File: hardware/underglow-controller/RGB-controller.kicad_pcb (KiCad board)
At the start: 4 copper layers, 86 x 97.7 mm, 142 parts, among them J2 U.FL-R-SMT-1(10), J3 DM3AT-SF-PEJM5, J4 DTM1312PA12PBR008, J5 Conn_01x10, J6 CONSOLE, J7 U.FL-R-SMT-1(10), J8 JTAG, Q2 Q_Dual_NMOS_S1G1S2G2D2D2D1D1, Q3 Q_Dual_NMOS_S1G1S2G2D2D2D1D1, Q4 Q_Dual_NMOS_S1G1S2G2D2D2D1D1, SW2 SW_Push, SW3 SW_Push, SW4 SW_Push, U10 DRV8844PWP, U11 RP2040, U2 ESP-PSRAM32, U3 SN65HVD230, U4 ESP32-S3R2, U5 W25Q128JVS, U6 WS2815B, U7 W25Q128JVS, U8 ADP2303ARDZ-3.3, U9 COM-13909, Y2 40MHZ, Y3 32.7k, Y4 40MHZ

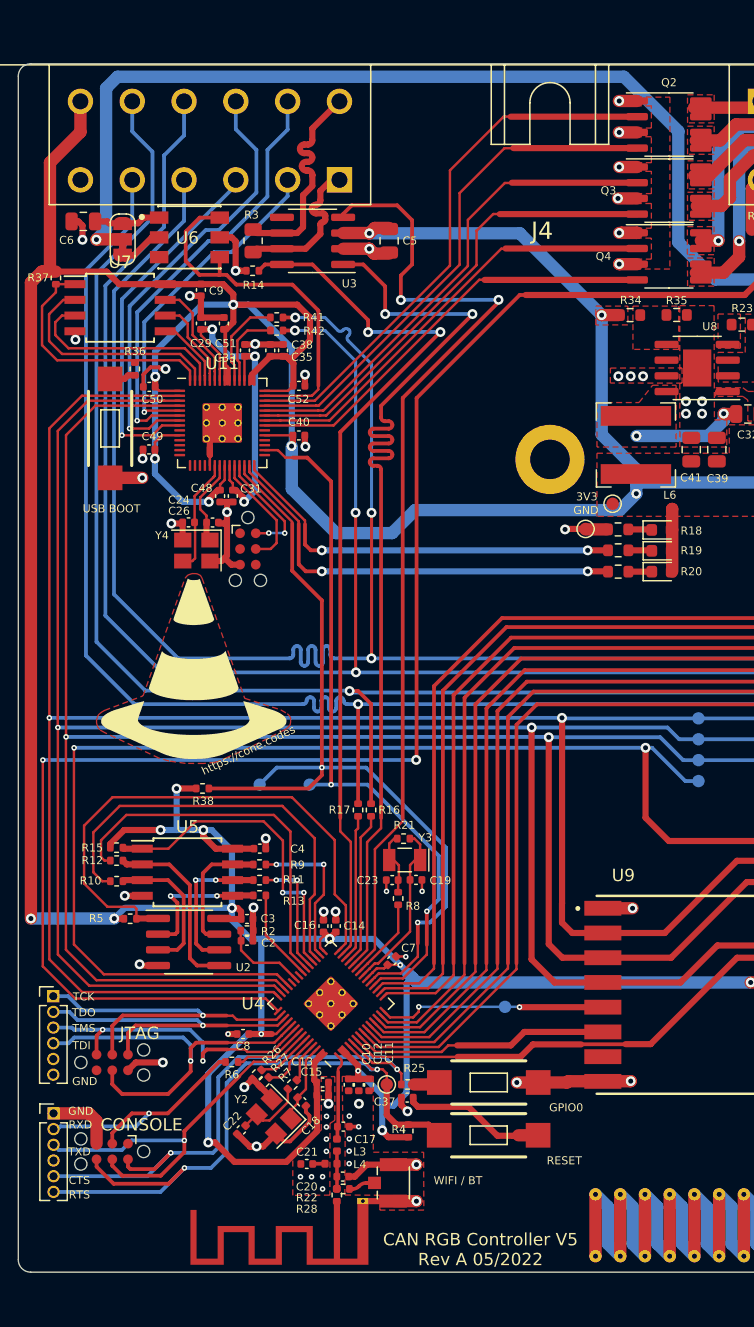
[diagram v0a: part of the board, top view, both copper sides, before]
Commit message: Update images and project names
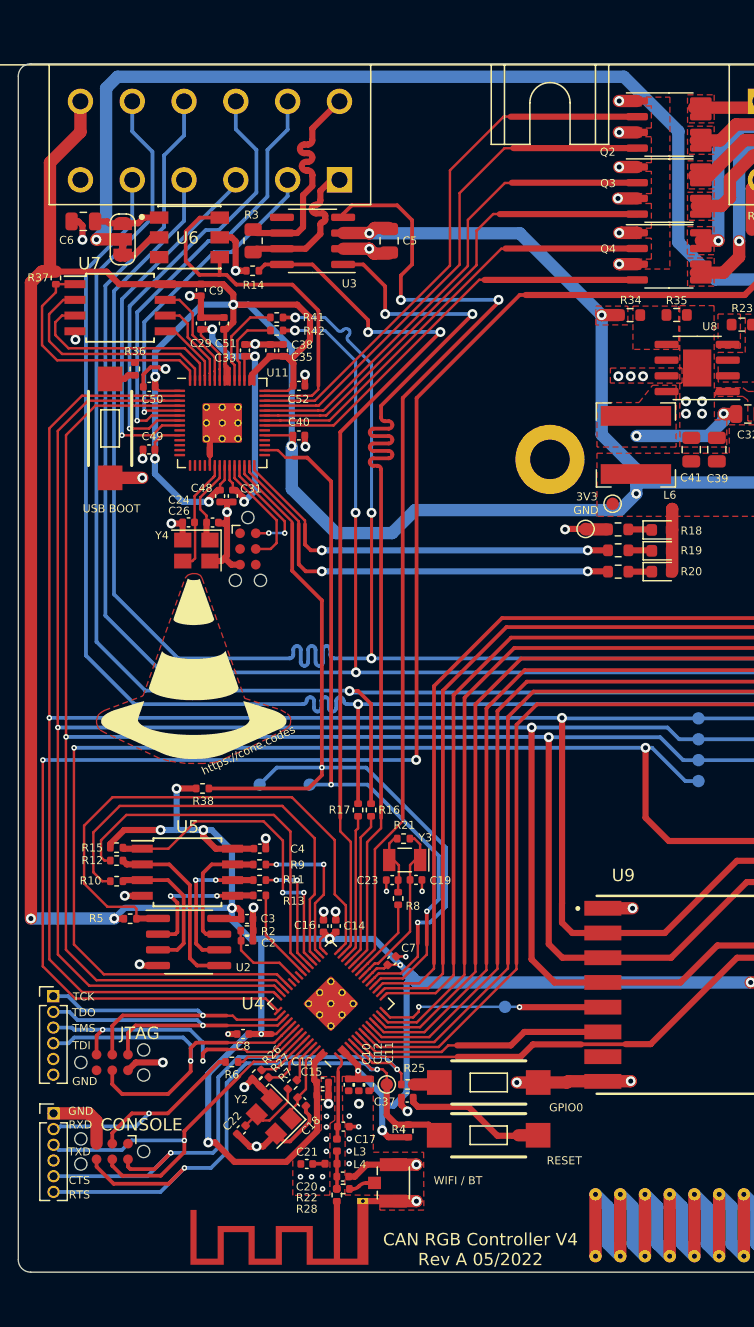
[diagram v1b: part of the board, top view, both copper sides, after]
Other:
- board text added: "CAN RGB Controller V4 Rev A 05/2022"
- board text removed: "CAN RGB Controller V5 Rev A 05/2022"
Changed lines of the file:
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@@
     (property "Sheetname" "")
     (attr through_hole)
-    (fp_text reference "J4" (at 0.63547 -8.51521 180) (layer "F.SilkS")
+    (fp_text reference "J4" (at 0.63547 -8.51521 180) (layer "F.SilkS") hide
       (effects (font (size 1.401024 1.401024) (thickness 0.15)))
     )
@@
     (property "exclude_from_bom" "")
     (attr smd exclude_from_pos_files exclude_from_bom)
-    (fp_text reference "Q4" (at -5.3 0 unlocked) (layer "F.SilkS")
+    (fp_text reference "Q4" (at -4.92 -0.61 unlocked) (layer "F.SilkS")
       (effects (font (size 0.65 0.65) (thickness 0.15)))
     )
@@
     (property "Sheetname" "")
     (attr smd)
-    (fp_text reference "U7" (at 0 -3.68) (layer "F.SilkS")
+    (fp_text reference "U7" (at -2.46 -3.57) (layer "F.SilkS")
       (effects (font (size 1 1) (thickness 0.15)))
     )
@@
     (property "exclude_from_bom" "")
     (attr smd exclude_from_pos_files exclude_from_bom)
-    (fp_text reference "Q3" (at -4.9 0 unlocked) (layer "F.SilkS")
+    (fp_text reference "Q3" (at -4.93 -0.58 unlocked) (layer "F.SilkS")
       (effects (font (size 0.65 0.65) (thickness 0.15)))
     )
@@
     (property "exclude_from_bom" "")
     (attr smd exclude_from_pos_files exclude_from_bom)
-    (fp_text reference "Q2" (at 0 -3.4 unlocked) (layer "F.SilkS")
+    (fp_text reference "Q2" (at -4.96 2.22 unlocked) (layer "F.SilkS")
       (effects (font (size 0.65 0.65) (thickness 0.15)))
     )
@@
     (property "Sheetname" "")
     (attr smd)
-    (fp_text reference "U11" (at 0 -4.82) (layer "F.SilkS")
-      (effects (font (size 1 1) (thickness 0.15)))
+    (fp_text reference "U11" (at 4.47 -4.06) (layer "F.SilkS")
+      (effects (font (size 0.65 0.65) (thickness 0.15)))
     )
     (fp_text value "RP2040" (at 0 4.82) (layer "F.Fab")
@@
     (effects (font (size 0.65 0.65) (thickness 0.15)))
   )
-  (gr_text "CAN RGB Controller V5\nRev A 05/2022" (at 61.38 137.9) (layer "F.SilkS")
+  (gr_text "CAN RGB Controller V4\nRev A 05/2022" (at 61.38 137.9) (layer "F.SilkS")
     (effects (font (size 1 1) (thickness 0.15)))
   )

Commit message: Radio hardware and software design
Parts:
- removed C2: 1uF, Capacitor_SMD:C_0402_1005Metric
- removed C3: 0.1uF, Capacitor_SMD:C_0402_1005Metric
- removed R2: 442k, Resistor_SMD:R_0402_1005Metric
- removed R5: 100k, Resistor_SMD:R_0402_1005Metric
- removed U2: ESP-PSRAM32, Package_SO:SOIC-8_3.9x4.9mm_P1.27mm
- AE2: value Antenna_Shield -> PCB_ANT
- AE3: value Antenna_Shield -> PCB_ANT_RFM69
- C17: value C_Small -> 4.6pF
- C18, C22: value C_Small -> 16pF
- C19, C23: value C_Small -> 10pF
- C20: value C_Small -> 4pF
- C21: value C_Small -> 2pF
- C24, C26: value C_Small -> 20pF
- D5: footprint Diode_SMD:D_SOD-123 -> Diode_SMD:D_SOD-123F
- L3: value L_Small -> 2nH
- L4: value L_Small -> 2.2nH
- Q2, Q3, Q4: value Q_Dual_NMOS_S1G1S2G2D2D2D1D1 -> STS8DNF3LL
- R23: value 100k -> 10k
- R39: footprint Resistor_SMD:R_0603_1608Metric -> Resistor_SMD:R_0402_1005Metric
- R41, R42: value 27R4 -> 27r4
- moved C14 0.46 mm to (49.7, 111.3)
- moved C16 0.46 mm to (48.7, 111.3)
- moved R12 0.31 mm to (32.0, 106.8)
- moved D5 0.28 mm to (89.6, 55.2)
- moved C40 0.11 mm to (46.6, 72.1)
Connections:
- U4 pad 36: /SPICLK_N -> unconnected-(U4-Pad36)
- U4 pad 37: /SPICLK_P -> unconnected-(U4-Pad37)
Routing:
- net /SPICS1: track 44.5 -> 0.00 mm
- net /SPIQ: track 14.8 -> 1.60 mm
- net /SPICLK: track 11.9 -> 1.73 mm, vias 2 -> 0
- net /SPIWP: track 11.6 -> 1.65 mm
- net /SPID: track 11.4 -> 1.70 mm, vias 2 -> 0
- net /SPIHD: track 10.5 -> 1.71 mm
- net /SPICLK_P: track 7.04 -> 0.00 mm
- net +3V3: track 540.5 -> 534.2 mm, vias 25 -> 32
- net GND: track 134.7 -> 129.9 mm, vias 80 -> 81
- net /GPIO_GPO5: track 38.3 -> 35.0 mm
- net /GPIO_GPO4: track 40.6 -> 38.2 mm
- net /GPIO_GPO1: track 45.3 -> 43.6 mm
- net /FSPICLK: track 217.0 -> 217.8 mm
- net /FSPID: track 225.5 -> 226.3 mm
- net /CHIP_PU: track 55.1 -> 55.8 mm
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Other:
- board text removed: "Module2A"
- board text removed: "Module2B"

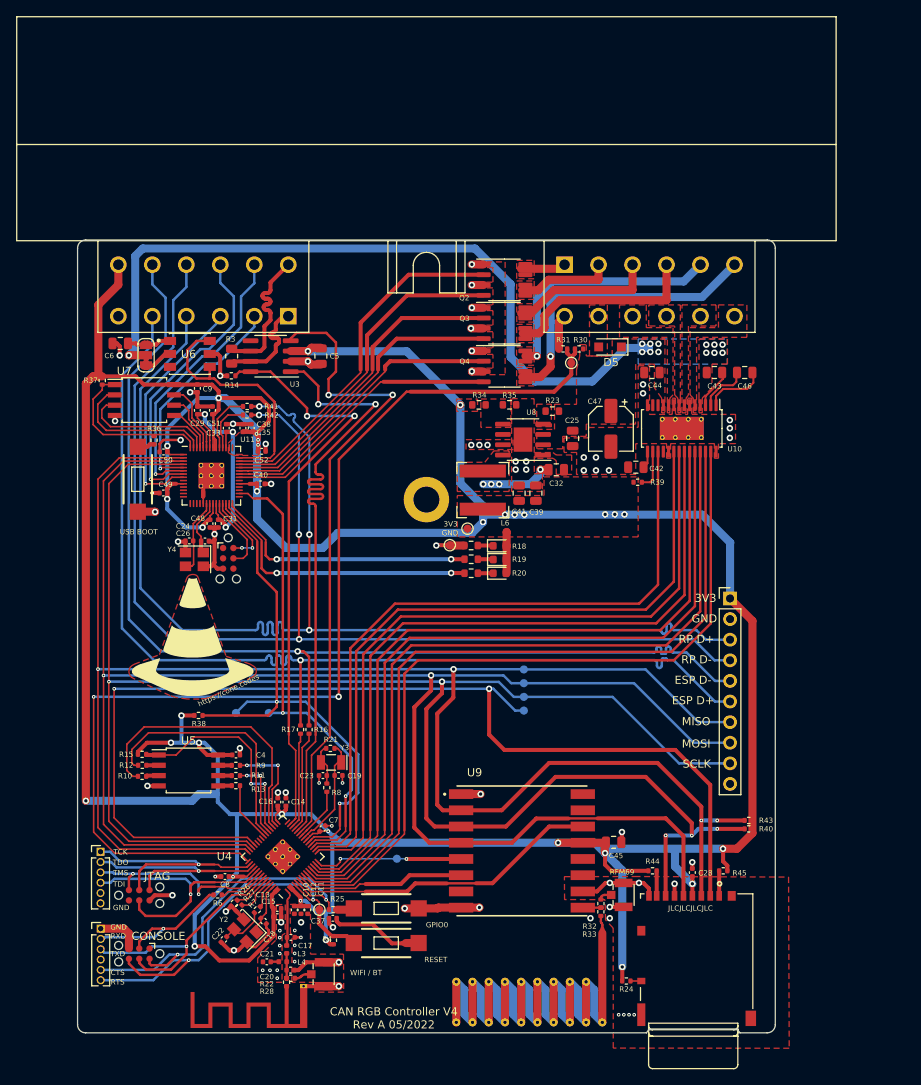
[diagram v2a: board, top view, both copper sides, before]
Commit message: hardware updates: fix SPI bus on pico and flatten radio module
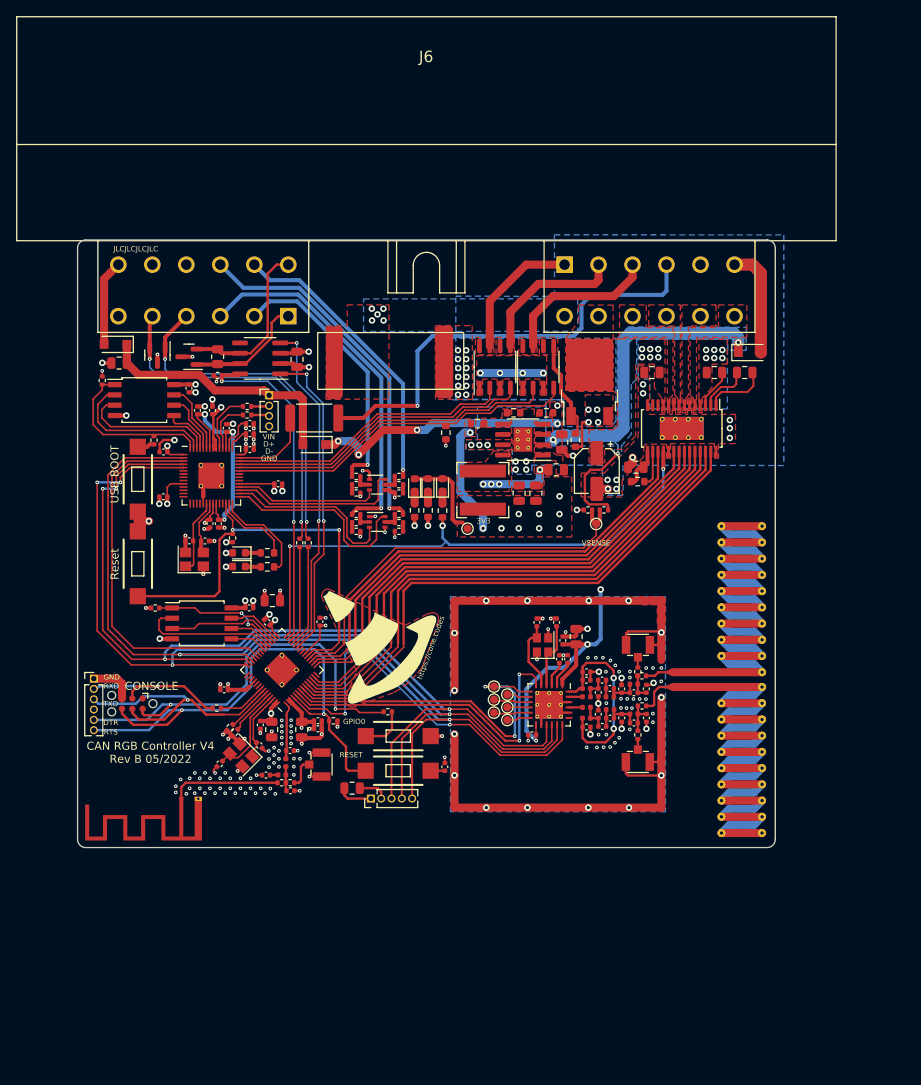
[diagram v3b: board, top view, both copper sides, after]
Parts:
- removed the C45 at (90.1, 116.3)
- removed the C6 at (29.3, 54.8)
- removed H1: MountingHole_Pad, MountingHole:MountingHole_3.2mm_M3_DIN965_Pad
- removed the J5 at (104.4, 86.2)
- removed JP2: LED Voltage Select, Jumper:SolderJumper-3_P1.3mm_Bridged12_RoundedPad1.0x1.5mm_NumberLabels
- removed the R13 at (43.5, 109.3)
- removed the R21 at (55.2, 104.7)
- removed the R3 at (43.0, 56.3)
- removed the R40 at (106.7, 114.6)
- removed the R43 at (106.7, 113.5)
- removed the R44 at (94.9, 119.8)
- removed the R45 at (103.6, 119.8)
- removed the R7 at (46.2, 124.6)
- removed the R8 at (54.7, 109.5)
- removed TC3, TC4: TC2030-IDC, Connector:Tag-Connect_TC2030-IDC-NL_2x03_P1.27mm_Vertical
- removed TP10: CS1, TestPoint:TestPoint_Pad_D1.0mm
- removed TP11: CS2, TestPoint:TestPoint_Pad_D1.0mm
- removed TP12: RP_RUN, TestPoint:TestPoint_Pad_D1.0mm
- removed the TP8 at (79.0, 96.6)
- removed the TP9 at (79.0, 100.0)
- removed the U6 at (37.8, 56.0)
- removed the U9 at (78.8, 117.3)
- added AE2: Antenna_Shield, RF_Antenna:Texas_SWRA416_868MHz_915MHz, F.Cu at (102.6, 86.3)
- added C16: 0.01uF, Capacitor_SMD:C_0402_1005Metric, F.Cu at (86.7, 96.3)
- added C17: C_Small, Capacitor_SMD:C_0402_1005Metric, F.Cu at (89.6, 97.3)
- added C18: C_Small, Capacitor_SMD:C_0402_1005Metric, F.Cu at (92.6, 97.8)
- added C20: 6.8pF, Capacitor_SMD:C_0402_1005Metric, F.Cu at (91.1, 97.3)
- added C21: 3.3pF, Capacitor_SMD:C_0402_1005Metric, F.Cu at (94.1, 97.3)
- added C22: 8.2pF, Capacitor_SMD:C_0402_1005Metric, F.Cu at (88.2, 97.8)
- added C24: 10uF, Capacitor_SMD:C_0805_2012Metric, F.Cu at (85.5, 90.9)
- added C25: 0.1uF, Capacitor_SMD:C_0402_1005Metric, F.Cu at (80.0, 103.0)
- added C26: 0.1uF, Capacitor_SMD:C_0402_1005Metric, F.Cu at (83.8, 91.4)
- added C27: 0.1uF, Capacitor_SMD:C_0402_1005Metric, F.Cu at (83.4, 93.7)
- added C29: 68pF, Capacitor_SMD:C_0402_1005Metric, F.Cu at (86.7, 102.0)
- added C30: C_Small, Capacitor_SMD:C_0402_1005Metric, F.Cu at (89.6, 100.9)
- added C31: C_Small, Capacitor_SMD:C_0402_1005Metric, F.Cu at (92.6, 101.5)
- added C32: 8.2pF, Capacitor_SMD:C_0402_1005Metric, F.Cu at (88.7, 102.0)
- added C33: 6.8pF, Capacitor_SMD:C_0402_1005Metric, F.Cu at (91.1, 100.9)
- added C34: 5.6pF, Capacitor_SMD:C_0402_1005Metric, F.Cu at (94.1, 100.9)
- added C35: C_Small, Capacitor_SMD:C_0402_1005Metric, F.Cu at (88.2, 100.5)
- added C36: 16pF, Capacitor_SMD:C_0402_1005Metric, F.Cu at (83.0, 89.1)
- added C37: 16pF, Capacitor_SMD:C_0402_1005Metric, F.Cu at (80.6, 89.1)
- added C64: 10uF, Capacitor_SMD:C_0805_2012Metric, F.Cu at (57.8, 109.6)
- added C65: 10uF, Capacitor_SMD:C_0805_2012Metric, F.Cu at (29.1, 57.2)
- added D10: PESD2CANFD24V-T, Package_TO_SOT_SMD:SOT-23, F.Cu at (33.8, 56.2)
- added D11: PESD2CANFD24V-T, Package_TO_SOT_SMD:SOT-23, F.Cu at (37.7, 56.4)
- added D4: GRN, LED_SMD:LED_0603_1608Metric, F.Cu at (67.2, 72.2)
- added D5: GRN, LED_SMD:LED_0603_1608Metric, F.Cu at (69.0, 72.2)
- added D7: D_Small, Diode_SMD:D_SOD-123F, F.Cu at (28.7, 54.9)
- added D9: D_Small, Diode_SMD:D_SOD-123F, F.Cu at (53.2, 67.2)
- added F2: Fuse, ConeCodes:Keystone-3587-10TR, F.Cu at (62.6, 56.4)
- added J7: Conn_01x04, Connector_PinHeader_1.27mm:PinHeader_1x04_P1.27mm_Vertical, F.Cu at (47.6, 61.1)
- added L2: 22nH, Inductor_SMD:L_0402_1005Metric, F.Cu at (86.7, 97.3)
- added L3: 2.7nH, Inductor_SMD:L_0402_1005Metric, F.Cu at (86.7, 98.3)
- added L4: 5.6nH, Inductor_SMD:L_0402_1005Metric, F.Cu at (89.6, 98.3)
- added L5: 5.6nH, Inductor_SMD:L_0402_1005Metric, F.Cu at (92.6, 96.8)
- added L6: 33nH, Inductor_SMD:L_0402_1005Metric, F.Cu at (86.7, 100.9)
- added L7: 3.9nH, Inductor_SMD:L_0402_1005Metric, F.Cu at (86.7, 99.6)
- added L8: 6.8nH, Inductor_SMD:L_0402_1005Metric, F.Cu at (89.6, 99.9)
- added L9: 6.8nH, Inductor_SMD:L_0402_1005Metric, F.Cu at (92.6, 100.4)
- added Q5: MBT3904DW1T1G, Package_TO_SOT_SMD:SOT-363_SC-70-6, F.Cu at (60.9, 76.8)
- added Q6: Q_PMOS_GDS, Package_TO_SOT_SMD:TO-252-2, F.Cu at (87.1, 59.5)
- added R23: 10k, Resistor_SMD:R_0603_1608Metric, F.Cu at (69.4, 65.7)
- added R25: 10k, Resistor_SMD:R_0402_1005Metric, F.Cu at (58.3, 71.1)
- added R26: 10k, Resistor_SMD:R_0402_1005Metric, F.Cu at (58.3, 75.8)
- added R27: 1k, Resistor_SMD:R_0402_1005Metric, F.Cu at (58.3, 72.2)
- added R28: 1k, Resistor_SMD:R_0402_1005Metric, F.Cu at (58.3, 76.8)
- added R29: 499R, Resistor_SMD:R_0402_1005Metric, F.Cu at (58.3, 73.2)
- added R30: 499R, Resistor_SMD:R_0402_1005Metric, F.Cu at (58.3, 77.9)
- added R31: 10k, Resistor_SMD:R_0402_1005Metric, F.Cu at (63.6, 75.8)
- added R34: 1k, Resistor_SMD:R_0402_1005Metric, F.Cu at (63.6, 76.8)
- added R35: 499R, Resistor_SMD:R_0402_1005Metric, F.Cu at (63.6, 73.2)
- added R36: 499R, Resistor_SMD:R_0402_1005Metric, F.Cu at (63.6, 77.9)
- added R37: 240R, Resistor_SMD:R_0603_1608Metric, F.Cu at (67.2, 75.3)
- added R38: 240R, Resistor_SMD:R_0603_1608Metric, F.Cu at (69.0, 75.4)
- added R46: 10k, Resistor_SMD:R_0603_1608Metric, F.Cu at (85.4, 66.7)
- added R47: 120,DNF, Resistor_SMD:R_0805_2012Metric, F.Cu at (41.3, 56.4)
- added SW3: SW_Push, ConeCodes:SW_RS-032G05A3-SMRT, F.Cu at (31.4, 81.9)
- added TP3: DIO1, TestPoint:TestPoint_Pad_D1.0mm, F.Cu at (77.0, 98.0)
- added TP7: DIO5, TestPoint:TestPoint_Pad_D1.0mm, F.Cu at (77.0, 101.2)
- added U4: SX1231HIMLTRT, Package_DFN_QFN:QFN-24-1EP_5x5mm_P0.65mm_EP3.4x3.4mm_ThermalVias, F.Cu at (82.1, 99.3)
- AE3: value PCB_ANT_RFM69 -> Antenna_Shield
- C12: renamed from C51; value 0.1uF -> 1uF
- C19: value 10pF -> 22pF
- C23: value 10pF -> C_Small
- C28: value 1uF -> 0.1uF
- C40: renamed from C12; footprint Capacitor_SMD:C_0402_1005Metric -> Capacitor_SMD:C_0805_2012Metric
- C42: renamed from C16; value 1uF -> 10uF; footprint Capacitor_SMD:C_0402_1005Metric -> Capacitor_SMD:C_0805_2012Metric
- C44: renamed from C15; footprint Capacitor_SMD:C_0402_1005Metric -> Capacitor_SMD:C_0805_2012Metric
- C5: renamed from C38; value 1uF -> 0.1uF
- J3: value DM3AT-SF-PEJM5 -> U.FL-R-SMT-1(10); footprint ConeCodes:HRS_DM3AT-SF-PEJM5 -> ConeCodes:HRS_U.FL-R-SMT-1(10)
- J8: value JTAG -> Conn_01x05; footprint Connector_PinHeader_1.27mm:PinHeader_1x06_P1.27mm_Vertical -> Connector_PinHeader_1.27mm:PinHeader_1x05_P1.27mm_Vertical
- L12: renamed from L6; value 6.8uh -> 4.7uH
- Q4: value STS8DNF3LL -> MBT3904DW1T1G; footprint Package_SO:SO-8_3.9x4.9mm_P1.27mm -> Package_TO_SOT_SMD:SOT-363_SC-70-6
- R24: value 10k -> 0R; footprint Resistor_SMD:R_0402_1005Metric -> Resistor_SMD:R_2512_6332Metric
- R32: value 0R -> 10k
- R33: value 0R -> 1k
- R39: footprint Resistor_SMD:R_0402_1005Metric -> Resistor_SMD:R_0603_1608Metric
- SW2: renamed from SW4; value SW_Push -> USB BOOT
- TP2: value CHIP_PU -> DIO0
- TP4: value 3V3OUT -> DIO2
- TP5: value MOSI -> DIO3; moved to F.Cu
- TP6: value MISO -> DIO4; moved to F.Cu
- TP8: renamed from TP3; value VBAT_SENSE -> VSENSE
- U8: footprint Package_SO:SOIC-8-1EP_3.9x4.9mm_P1.27mm_EP2.29x3mm -> Package_SO:SOIC-8-1EP_3.9x4.9mm_P1.27mm_EP2.29x3mm_ThermalVias
- Y2: renamed from Y4; value 40MHZ -> 12MHZ
- Y3: value 32.7k -> 32mhz; footprint Crystal:Crystal_SMD_MicroCrystal_CC7V-T1A-2Pin_3.2x1.5mm -> Crystal:Crystal_SMD_2520-4Pin_2.5x2.0mm
- moved R24 79.3 mm to (53.2, 63.9)
- moved R10 62.5 mm to (93.1, 95.2), turned to 90 degrees
- moved R12 61.2 mm to (93.1, 103.0), turned to -90 degrees
- moved R33 58.2 mm to (63.6, 72.2), turned to 0 degrees
- moved R32 58.2 mm to (63.6, 71.1), turned to 180 degrees
- moved R9 51.3 mm to (93.6, 95.7), turned to 180 degrees
- moved R11 50.8 mm to (93.6, 99.4), turned to 180 degrees
- moved AE3 35.0 mm to (102.6, 106.1), turned to -90 degrees
- moved TP2 34.9 mm to (75.3, 97.0), turned to 90 degrees
- moved C23 34.9 mm to (86.7, 95.2), turned to 0 degrees
- moved C19 34.6 mm to (88.7, 96.2)
- moved J8 34.0 mm to (60.2, 110.8), turned to 90 degrees
- moved D2 32.2 mm to (43.9, 80.6), turned to 180 degrees
- moved D3 32.1 mm to (43.9, 82.3), turned to 180 degrees
- moved J2 30.9 mm to (93.1, 91.9), turned to 0 degrees
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- renumbered AE2 to AE4, C50 to C10, C33 to C11, C9 to C13, C26 to C14, C24 to C15, C29 to C2, C31 to C3, C10 to C38, C11 to C39, C35 to C4, C14 to C41, C13 to C43, C8 to C45, C7 to C46, C17 to C47, C20 to C48, C21 to C49, C4 to C50, C37 to C51, C18 to C52, C22 to C53, C46 to C54, C43 to C55, C44 to C56, C47 to C57, C42 to C58, C32 to C59, C52 to C6, C39 to C60, C41 to C61, C25 to C62, C5 to C63, C40 to C7, C48 to C8, C49 to C9, D4 to D2, D2 to D6, D5 to D8, J6 to J4, J7 to J5, J4 to J6, L3 to L10, L4 to L11, R4 to R13, R6 to R14, R16 to R15, R17 to R16, R22 to R17, R15 to R18, R28 to R19, R41 to R2, R25 to R20, R26 to R21, R27 to R22, R42 to R3, R37 to R4, R30 to R40, R31 to R41, R23 to R42, R34 to R43, R35 to R44, R18 to R45, R14 to R48, R36 to R5, R20 to R6, R19 to R7, R38 to R8, SW2 to SW4, SW3 to SW5, TP7 to TP9, U7 to U2, U11 to U3, U4 to U5, U5 to U6, U10 to U7, U3 to U9, Y2 to Y4
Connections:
- net /BST renamed /Power/BST
- net /CP1 renamed /Motor-Control/CP1
- net /CP2 renamed /Motor-Control/CP2
- net /DRV_RESET renamed /MCPWM_RESET
- net /DRV_SLEEP renamed /MCPWM_SLEEP
- net /EN1 renamed /MCPWM0_ENA
- net /EN2 renamed /MCPWM0_ENB
- net /EN3 renamed /MCPWM1_ENA
- net /EN4 renamed /MCPWM1_ENB
- net /FB renamed /Power/FB
- net /GPIO0_BOOTSTRAP renamed /ESP32-S3/GPIO0_BOOTSTRAP
- net /GPIO10 renamed /MCPWM1_INB
- net /GPIO14 renamed /RP2040_EN
- net /GPIO21 renamed /CAN_EN
- net /GPIO3 renamed /MCPWM0_INA
- net /GPIO45 renamed /ESP32-S3/GPIO45
- net /GPIO46 renamed /ESP32-S3/GPIO46
- net /GPIO5 renamed /MCPWM0_INB
- net /GPIO7 renamed /MCPWM1_INA
- net /GPIO_USB_D_N renamed /ESP32-S3/GPIO19
- net /GPIO_USB_D_P renamed /ESP32-S3/GPIO20
- net /GPO1 renamed /Connectors/GPO1
- net /GPO2 renamed /Connectors/GPO2
- net /GPO3 renamed /Connectors/GPO3
- net /LED_GREEN renamed /Pico Remote Proc/LED_GREEN
- net /LED_RED renamed /Pico Remote Proc/LED_RED
- net /LNA_IN renamed /ESP32-S3/LNA_IN
- net /MOTOR1_OUT1 renamed /Connectors/MOTOR1_OUT1
- net /MOTOR1_OUT2 renamed /Connectors/MOTOR1_OUT2
- net /MOTOR2_OUT1 renamed /Connectors/MOTOR2_OUT1
- net /MOTOR2_OUT2 renamed /Connectors/MOTOR2_OUT2
- net /PGOOD renamed /Power/PGOOD
- net /RF_ANT renamed /ESP32-S3/RF_ANT
- net /RF_ANT_EXT renamed /ESP32-S3/RF_ANT_EXT
- net /RP_SCLK renamed /Pico Remote Proc/RP_SCLK
- net /RP_SD0 renamed /Pico Remote Proc/RP_SD0
- net /RP_SD1 renamed /Pico Remote Proc/RP_SD1
- net /RP_SD2 renamed /Pico Remote Proc/RP_SD2
- net /RP_SD3 renamed /Pico Remote Proc/RP_SD3
- net /RP_SS renamed /Pico Remote Proc/RP_SS
- net /RP_USB_D_M renamed /Pico Remote Proc/RP_USB_D_N
- net /RP_USB_D_P renamed /Pico Remote Proc/RP_USB_D_P
- net /RXD renamed /ESP32-S3/RXD
- net /SPICS0 renamed /ESP32-S3/SPICS0
- net /SW renamed /Power/SW
- net /TXD renamed /ESP32-S3/TXD
- net /USB_BOOT renamed /Pico Remote Proc/USB_BOOT
- net /USB_D_P renamed /Connectors/USB_D_N
- net /XTAL_P renamed /ESP32-S3/XTAL_P
- net Net-(C43-Pad1) renamed /Motor-Control/VCP
- AE3 pad 1: /RF69_RF_ANT_PCB -> Net-(AE3-Pad1)
- C14 pad 1: /RP_XIN -> /Pico Remote Proc/RP_XIN
- C15 pad 1: /RP_XOUT -> /Pico Remote Proc/RP_XOUT
- C19 pad 1: /RTC_XTAL_P -> Net-(C19-Pad1)
- C19 pad 2: GND -> Net-(C17-Pad2)
- C23 pad 1: /RTC_XTAL_N -> /SX1276/VR_PA
- C28 pad 1: +3V3 -> /SX1276/VR_ANA
- C53 pad 1: /XTAL_N -> /ESP32-S3/XTAL_N
- C55 pad 2: /VIN -> /Connectors/VOUT
- C56 pad 1: /VIN -> /Connectors/VOUT
- C57 pad 1: /VIN -> /Connectors/VOUT
- C58 pad 1: Net-(C42-Pad1) -> /Motor-Control/V3P3OUT
- D8 pad 2: /VBAT -> /Connectors/IGNITION
- J2 pad 2: /RF69_RF_EXT -> Net-(J2-Pad2)
- J3 pad 1: /SD_D2 -> GND
- J3 pad 2: /FSPICS0 -> Net-(J3-Pad2)
- J3 pad 3: /FSPIQ -> GND
- J4 pad 5: /CTS -> /ESP32-S3/CTS
- J4 pad 6: /CHIP_PU -> /ESP32-S3/CHIP_PU
- J6 pad A11: /VBAT -> /Connectors/VOUT
- J6 pad A12: GND -> /Connectors/FUSE_IN
- J6 pad A4: /GPO4 -> /Connectors/LEDA
- J6 pad A5: /GPO6 -> GND
- J6 pad A6: /GPO5 -> /Connectors/IGNITION
- J6 pad B10: /CONN_B10 -> /Connectors/GPI3
- J6 pad B11: /CONN_B11 -> /Connectors/GPI1
- J6 pad B2: /CONN_B2 -> /Connectors/GPI2
- J6 pad B3: /CONN_B3 -> /Connectors/GPI4
- J6 pad B4: /CONN_RP_USB_D_P -> /Connectors/USB_D_P
- J6 pad B7: +3V3 -> Net-(D7-Pad2)
- J6 pad B8: /USB_D_N -> unconnected-(J6-PadB8)
- J6 pad B9: /CONN_RP_USB_D_N -> unconnected-(J6-PadB9)
- J8 pad 1: /MTCK -> +3V3
- J8 pad 2: /MTDO -> GND
- J8 pad 3: /MTMS -> /SCLK
- J8 pad 4: /MTDI -> /MISO
- J8 pad 5: GND -> /MOSI
- Q3 pad 5: /GPO4 -> /External-IO/VOUT_EN
- Q3 pad 6: /GPO4 -> /External-IO/VOUT_EN
- Q4 pad 2: /GPIO_GPO6 -> Net-(Q4-Pad2)
- Q4 pad 3: GND -> /GPIO_GPI1
- Q4 pad 4: /GPIO_GPO5 -> GND
- Q4 pad 5: /GPO5 -> Net-(Q4-Pad5)
- Q4 pad 6: /GPO5 -> /GPIO_GPI2
- R10 pad 1: /SPIWP -> Net-(C18-Pad1)
- R10 pad 2: Net-(R10-Pad2) -> Net-(J2-Pad2)
- R11 pad 1: /SPICLK -> Net-(AE3-Pad1)
- R11 pad 2: Net-(R11-Pad2) -> Net-(C31-Pad1)
- R12 pad 1: /SPIQ -> Net-(C31-Pad1)
- R12 pad 2: Net-(R12-Pad2) -> Net-(J3-Pad2)
- R13 pad 1: /CHIP_PU -> /ESP32-S3/CHIP_PU
- R15 pad 2: /USB_D_N -> /Connectors/USB_D_P
- R2 pad 1: /CONN_RP_USB_D_P -> /Connectors/CONN_RP_USB_D_P
- R20 pad 1: /CTS -> /ESP32-S3/CTS
- R24 pad 1: +3V3 -> /LEDA
- R24 pad 2: Net-(J3-PadSWA) -> /Connectors/LEDA
- R3 pad 1: /CONN_RP_USB_D_N -> /Connectors/CONN_RP_USB_D_N
- R32 pad 1: /RF69_RF_ANT -> /Connectors/GPI1
- R32 pad 2: /RF69_RF_EXT -> Net-(Q4-Pad5)
- R33 pad 1: /RF69_RF_ANT -> Net-(Q4-Pad5)
- R33 pad 2: /RF69_RF_ANT_PCB -> Net-(R33-Pad2)
- R39 pad 1: +3V3 -> /Motor-Control/V3P3OUT
- R40 pad 2: /GPIO38 -> /VSENSE
- R41 pad 1: /GPIO38 -> /VSENSE
- R9 pad 1: /SPIHD -> Net-(AE2-Pad1)
- R9 pad 2: Net-(R9-Pad2) -> Net-(C18-Pad1)
- SW4 pad 1: /CHIP_PU -> /ESP32-S3/CHIP_PU
- TC2 pad 2: /CTS -> /ESP32-S3/CTS
- TC2 pad 6: /CHIP_PU -> /ESP32-S3/CHIP_PU
- TP2 pad 1: /CHIP_PU -> /SX1276_IRQ
- TP4 pad 1: GND -> /SX1276/DIO2
- TP5 pad 1: /FSPID -> /SX1276/DIO3
- TP6 pad 1: /FSPIQ -> /SX1276/DIO4
- TP8 pad 1: /GPIO38 -> /VSENSE
- U3 pad 2: /FSPIQ -> /MOSI
- U3 pad 20: /RP_XIN -> /Pico Remote Proc/RP_XIN
- U3 pad 21: /RP_XOUT -> /Pico Remote Proc/RP_XOUT
- U3 pad 24: /RP_SWCLK -> unconnected-(U3-Pad24)
- U3 pad 25: /RP_SWD -> unconnected-(U3-Pad25)
- U3 pad 29: unconnected-(U11-Pad29) -> /GPIO_GPI4
- U3 pad 3: /FSPICLK -> /CS2
- U3 pad 30: /FSPICS2 -> /GPIO_GPI3
- U3 pad 31: unconnected-(U11-Pad31) -> /GPIO_GPI2
- U3 pad 32: unconnected-(U11-Pad32) -> /GPIO_GPI1
- U3 pad 4: /FSPID -> /SCLK
- U3 pad 5: /CONN_B2 -> /MISO
- U3 pad 6: /CONN_B11 -> unconnected-(U3-Pad6)
- U3 pad 7: /CONN_B10 -> unconnected-(U3-Pad7)
- U3 pad 8: /CONN_B3 -> unconnected-(U3-Pad8)
- U5 pad 14: /FSPICS1 -> unconnected-(U5-Pad14)
- U5 pad 18: /FSPICS2 -> /VSENSE
- U5 pad 21: /RTC_XTAL_P -> /ESP32-S3/RTC_XTAL_P
- U5 pad 22: Net-(R8-Pad2) -> /ESP32-S3/RTC_XTAL_N
- U5 pad 23: /GPIO_CAN_N -> /GPIO_CAN_P
- U5 pad 24: /GPIO_CAN_P -> /GPIO_CAN_N
- U5 pad 28: /SPICS1 -> /MCPWM_FAULT
- U5 pad 30: Net-(R9-Pad2) -> /ESP32-S3/SPIHD
- U5 pad 31: Net-(R10-Pad2) -> /ESP32-S3/SPIWP
- U5 pad 33: Net-(R11-Pad2) -> /ESP32-S3/SPICLK
- U5 pad 34: Net-(R12-Pad2) -> /ESP32-S3/SPIQ
- U5 pad 35: Net-(R13-Pad2) -> /ESP32-S3/SPID
- U5 pad 38: /FSPIHD -> /CS2
- U5 pad 39: /FSPICS0 -> /ESP32-S3/GPIO34
- U5 pad 4: /CHIP_PU -> /ESP32-S3/CHIP_PU
- U5 pad 40: /FSPID -> /MOSI
- U5 pad 41: /FSPICLK -> /SCLK
- U5 pad 42: /FSPIQ -> /MISO
- U5 pad 43: /GPIO38 -> unconnected-(U5-Pad43)
- U5 pad 44: /MTCK -> /ESP32-S3/MTCK
- U5 pad 45: /MTDO -> /ESP32-S3/MTDO
- U5 pad 47: /MTDI -> /ESP32-S3/MTDI
- U5 pad 48: /MTMS -> /ESP32-S3/MTMS
- U5 pad 5: /CTS -> /CS1
- U5 pad 53: Net-(R7-Pad2) -> /ESP32-S3/XTAL_N
- U5 pad 6: /GPIO1 -> /SX1276_RESET
- U5 pad 7: /GPIO2 -> /SX1276_IRQ
- U6 pad 2: /SPIQ -> /ESP32-S3/SPIQ
- U6 pad 3: /SPIWP -> /ESP32-S3/SPIWP
- U6 pad 5: /SPID -> /ESP32-S3/SPID
- U6 pad 6: /SPICLK -> /ESP32-S3/SPICLK
- U6 pad 7: /SPIHD -> /ESP32-S3/SPIHD
- U7 pad 11: /VIN -> /Connectors/VOUT
- U7 pad 15: Net-(C42-Pad1) -> /Motor-Control/V3P3OUT
- U7 pad 18: unconnected-(U10-Pad18) -> /MCPWM_FAULT
- U7 pad 4: /VIN -> /Connectors/VOUT
- Y2 pad 1: /RP_XOUT -> /Pico Remote Proc/RP_XIN
- Y2 pad 3: /RP_XIN -> /Pico Remote Proc/RP_XOUT
- Y3 pad 1: /RTC_XTAL_P -> /SX1276/RADIO_XTAL_P
- Y3 pad 2: /RTC_XTAL_N -> GND
- Y4 pad 3: /XTAL_N -> /ESP32-S3/XTAL_N
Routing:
- net +3V3: track 534.2 -> 136.4 mm, vias 32 -> 37
- net /FSPID: track 226.3 -> 0.00 mm, vias 5 -> 0
- net /FSPIQ: track 226.3 -> 0.00 mm, vias 4 -> 0
- net /FSPICLK: track 217.8 -> 0.00 mm, vias 2 -> 0
- net /CONN_RP_USB_D_P: track 153.1 -> 0.00 mm, vias 3 -> 0
- net /CONN_RP_USB_D_N: track 152.7 -> 0.00 mm, vias 3 -> 0
- net /USB_D_N: track 136.0 -> 0.00 mm, vias 1 -> 0
- net /FSPICS0: track 135.4 -> 0.00 mm, vias 2 -> 0
- net /GPIO38: track 134.2 -> 0.00 mm, vias 2 -> 0
- net /SCLK: track 0.00 -> 122.2 mm, vias 0 -> 4
- net /MISO: track 0.00 -> 122.1 mm, vias 0 -> 4
- net /MOSI: track 0.00 -> 117.4 mm, vias 0 -> 2
- net GND: track 129.9 -> 226.9 mm, vias 81 -> 195
- net /Connectors/USB_D_N: track 132.7 -> 44.0 mm, vias 1 -> 2
- net /MCPWM_FAULT: track 0.00 -> 68.3 mm, vias 0 -> 3
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- added copper zone on In2.Cu, net +3V3
- added copper zone on B.Cu, net /Connectors/FUSE_IN
- added copper zone on F.Cu, net /Connectors/FUSE_IN
- added copper zone on B.Cu, net /Connectors/FUSE_OUT
- added copper zone on F.Cu, net /Connectors/FUSE_OUT
- added copper zone on B.Cu, net /Connectors/VOUT
- added copper zone on F.Cu, net /Connectors/VOUT
- added copper zone on In2.Cu, net /Connectors/VOUT
- added copper zone on F.Cu, net /External-IO/VOUT_EN
- added copper zone on B.Cu, net GND
- removed copper zone on F.Cu, net /GPO4
- removed copper zone on F.Cu, net /GPO5
- removed copper zone on F.Cu, net /GPO6
- removed copper zone on F.Cu, net /VBAT
- removed copper zone on In2.Cu, net /VIN
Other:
- board size 86 x 97.7 mm -> 86 x 74.9 mm
- board text added: "BLUE"
- board text added: "CAN RGB Controller V4 Rev B 05/2022"
- board text added: "D+"
- board text added: "D-"
- board text added: "DTR"
- board text added: "GPI1"
- board text added: "GPI2"
- board text added: "GPI3"
- board text added: "GPI4"
- board text added: "GREEN"
- board text added: "IGN"
- board text added: "RED"
- board text added: "Reset"
- board text added: "USB D+"
- board text added: "USB D-"
- board text added: "VIN"
- board text added: "VOUT"
- board text added: "VSENSE"
- board text added: "vout"
- board text removed: "CAN RGB Controller V4 Rev A 05/2022"
- board text removed: "CS0"
- board text removed: "CS1"
- board text removed: "CS2"
- board text removed: "CTS"
- board text removed: "ESP D+"
- board text removed: "ESP D-"
- board text removed: "GPO1"
- board text removed: "GPO2"
- board text removed: "GPO3"
- board text removed: "GPO4"
- board text removed: "GPO5"
- board text removed: "GPO6"
- board text removed: "JTAG"
- board text removed: "MISO"
- board text removed: "MOSI"
- board text removed: "RFM69"
- board text removed: "RP D+"
- board text removed: "RP D-"
- board text removed: "RP2040 RUN"
- board text removed: "SCL"
- board text removed: "SCLK"
- board text removed: "SDA"
- board text removed: "TCK"
- board text removed: "TDI"
- board text removed: "TDO"
- board text removed: "TMS"
- board text removed: "TTL 3V3"
- board text removed: "USB0 D+"
- board text removed: "USB0 D-"
- board text removed: "USB1 D+"
- board text removed: "USB1 D-"
- board text removed: "WIFI / BT"

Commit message: god i wish i remembered what this was
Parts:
- removed D4: GRN, LED_SMD:LED_0603_1608Metric
- removed R37: 240R, Resistor_SMD:R_0603_1608Metric
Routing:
- net Net-(D4-Pad1): track 1.50 -> 0.00 mm
- net GND: track 226.9 -> 225.8 mm, vias 195 -> 194
- net /MISO: track 122.1 -> 122.8 mm
- net /MOSI: track 117.4 -> 118.0 mm
- net /SCLK: track 122.2 -> 122.8 mm
